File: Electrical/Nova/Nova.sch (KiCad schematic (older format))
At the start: 0 parts

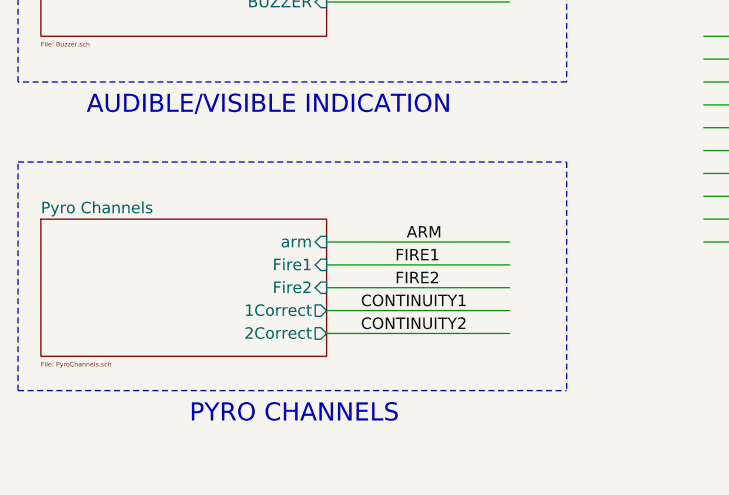
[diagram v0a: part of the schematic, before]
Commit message: Added Third Pyro
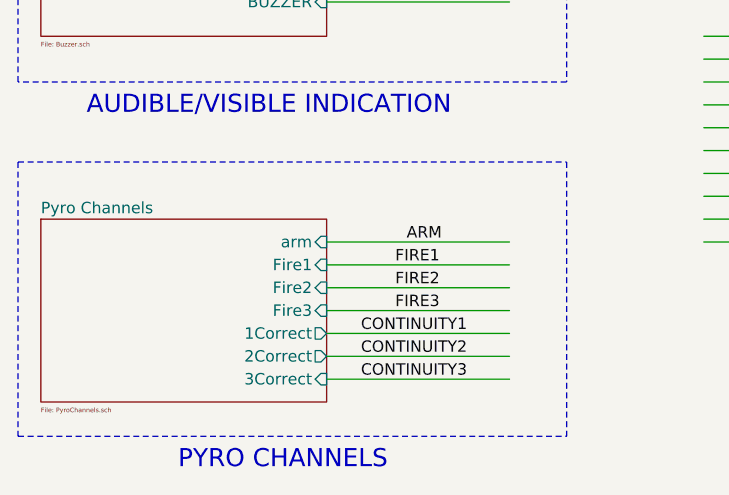
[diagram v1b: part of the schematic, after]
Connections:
- net labels added: CONTINUITY3, FIRE3
- wire segments 99 -> 101
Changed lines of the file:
@@
 $Descr USLetter 11000 8500
 encoding utf-8
-Sheet 1 20
+Sheet 1 21
 Title ""
 Date ""
@@
 	2050 6400 2850 6400
 Wire Wire Line
-	2050 6500 2850 6500
-Wire Wire Line
 	2050 6600 2850 6600
+Wire Wire Line
+	2050 6700 2850 6700
 Text Label 2400 6200 0    50   ~ 0
 ARM
@@
 Text Label 2350 6400 0    50   ~ 0
 FIRE2
-Text Label 2200 6500 0    50   ~ 0
+Text Label 2200 6600 0    50   ~ 0
 CONTINUITY1
-Text Label 2200 6600 0    50   ~ 0
+Text Label 2200 6700 0    50   ~ 0
 CONTINUITY2
 Wire Notes Line
@@
 	700  5850 3100 5850
 Wire Notes Line
-	3100 5850 3100 6850
-Wire Notes Line
-	700  6850 700  5850
-Wire Notes Line
-	700  6850 3100 6850
-Text Notes 1450 7000 0    79   ~ 0
+	700  7050 3100 7050
+Text Notes 1400 7200 0    79   ~ 0
 PYRO CHANNELS
 Wire Notes Line
@@
 	6800 5300 7350 5300
 $Sheet
-S 800  6100 1250 600
+S 800  6100 1250 800
 U 5F448D4B
 F0 "Pyro Channels" 50
@@
 F2 "arm" I R 2050 6200 50
 F3 "Fire1" I R 2050 6300 50
-F4 "1Correct" O R 2050 6500 50
+F4 "1Correct" O R 2050 6600 50
 F5 "Fire2" I R 2050 6400 50
-F6 "2Correct" O R 2050 6600 50
-$EndSheet
+F6 "2Correct" O R 2050 6700 50
+F7 "Fire3" I R 2050 6500 50
+F8 "3Correct" I R 2050 6800 50
+$EndSheet
+Wire Notes Line
+	3100 5850 3100 7050
+Wire Notes Line
+	700  5850 700  7050
+Wire Wire Line
+	2050 6500 2850 6500
+Wire Wire Line
+	2050 6800 2850 6800
+Text Label 2350 6500 0    50   ~ 0
+FIRE3
+Text Label 2200 6800 0    50   ~ 0
+CONTINUITY3
 $EndSCHEMATC

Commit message: Cleaned Up Schematic & Folder for Project
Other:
- note added: "Nova Flight Computer: Rev 1"
- note added: "PIN HEADERS"

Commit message: Changes Galore
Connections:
- net labels added: CS_FLASH, IO0, IO1, IO2, IO3
- net labels removed: HOLD, WP
- no-connect marks 32 -> 30
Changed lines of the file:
@@
 Text Label 8800 950  2    50   ~ 0
 SCLK
-Text Label 8800 1050 2    50   ~ 0
-MOSI
-Text Label 8800 1150 2    50   ~ 0
-MISO
 Text Label 8800 1250 2    50   ~ 0
 BAROMETER_CS
@@
 Text Label 8800 1600 2    50   ~ 0
 SCLK
-Text Label 8800 1700 2    50   ~ 0
-MOSI
-Text Label 8800 1800 2    50   ~ 0
-MISO
 Text Label 8800 1900 2    50   ~ 0
 GYRO_ACCEL_CS
@@
 Text Label 8800 2650 2    50   ~ 0
 SCLK
-Text Label 8800 2550 2    50   ~ 0
-MOSI
-Text Label 8800 2450 2    50   ~ 0
-MISO
 Text Label 8800 2350 2    50   ~ 0
 ACCELEROMETER_CS
@@
 Wire Notes Line
 	3000 5950 3000 4900
-NoConn ~ 8100 4450
-$Sheet
-S 8900 3200 1250 500
-U 5F3B5BD1
-F0 "MicroSD" 50
-F1 "../Common_Modules/FHSD/Flash SD Board/Micro SD.sch" 20
-F2 "MISO" I L 8900 3300 50
-F3 "MOSI" I L 8900 3400 50
-F4 "SCLK" I L 8900 3500 50
-F5 "CS_SD" I L 8900 3600 50
-$EndSheet
-$Sheet
-S 8900 3850 1250 700
-U 5F3B5C2E
-F0 "FlashChip" 50
-F1 "../Common_Modules/FHSD/Flash SD Board/Flash Chip.sch" 20
-F2 "SCLK" I L 8900 3950 50
-F3 "MOSI" I L 8900 4050 50
-F4 "MISO" I L 8900 4150 50
-F5 "CS_FLASH" I L 8900 4250 50
-F6 "HOLD" I L 8900 4350 50
-F7 "WP" I L 8900 4450 50
-$EndSheet
 Text Notes 8900 3100 0    79   ~ 0
 SENSORS\n\n
@@
 DATA LOGGING\n
 Text Label 8800 4250 2    50   ~ 0
-FLASH_CS
+IO2
 Text Label 8800 3600 2    50   ~ 0
 SD_CS
 Text Label 8800 4450 2    50   ~ 0
-WP
+CS_FLASH
 Text Label 8800 4350 2    50   ~ 0
-HOLD
-Text Label 8800 4150 2    50   ~ 0
-MISO
-Text Label 8800 4050 2    50   ~ 0
-MOSI
+IO3
 Text Label 8800 3950 2    50   ~ 0
 SCLK
@@
 F21 "20" I R 2150 6450 50
 $EndSheet
-NoConn ~ 8100 4350
 Wire Notes Line
 	8000 3050 8000 4650
@@
 Text Notes 3350 6000 0    197  ~ 39
 Nova Flight Computer: Rev 1
+Text Label 8800 4150 2    50   ~ 0
+IO1
+Text Label 8800 4050 2    50   ~ 0
+IO0
+$Sheet
+S 8900 3850 1250 700
+U 5F3B5C2E
+F0 "FlashChip" 50
+F1 "../Common_Modules/FHSD/Flash SD Board/Flash Chip.sch" 20
+F2 "SCLK" I L 8900 3950 50
+F3 "IO0" I L 8900 4050 50
+F4 "IO1" I L 8900 4150 50
+F5 "CS_FLASH" I L 8900 4450 50
+F6 "IO3" I L 8900 4350 50
+F7 "IO2" I L 8900 4250 50
+$EndSheet
+$Sheet
+S 8900 3200 1250 500
+U 5F3B5BD1
+F0 "MicroSD" 50
+F1 "../Common_Modules/FHSD/Flash SD Board/Micro SD.sch" 20
+F2 "MISO" I L 8900 3300 50
+F3 "MOSI" I L 8900 3400 50
+F4 "SCLK" I L 8900 3500 50
+F5 "CS_SD" I L 8900 3600 50
+$EndSheet
+Text Label 8800 2550 2    50   ~ 0
+MOSI
+Text Label 8800 2450 2    50   ~ 0
+MISO
+Text Label 8800 1700 2    50   ~ 0
+MOSI
+Text Label 8800 1800 2    50   ~ 0
+MISO
+Text Label 8800 1150 2    50   ~ 0
+MISO
+Text Label 8800 1050 2    50   ~ 0
+MOSI
 $EndSCHEMATC

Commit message: Crossing Fingers Github
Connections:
- wire segments 101 -> 102
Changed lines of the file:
@@
 $Descr USLetter 11000 8500
 encoding utf-8
-Sheet 1 21
+Sheet 1 22
 Title ""
 Date ""
@@
 	8000 3050 10250 3050
 Wire Notes Line
-	10250 4900 10250 5650
-Wire Notes Line
 	750  6200 3000 6200
 Wire Notes Line
@@
 Wire Wire Line
 	2150 2450 2900 2450
-Wire Notes Line
-	8000 5650 8000 4900
-Text Notes 8750 5800 0    79   ~ 0
+Text Notes 8750 6300 0    79   ~ 0
 POWER SUPPLY\n
 $Sheet
-S 8700 5050 1000 500
+S 8900 5050 1250 550
 U 5F3B0B4B
 F0 "PowerSupply" 50
@@
 	8000 4900 10250 4900
 Wire Notes Line
-	8000 5650 10250 5650
+	8000 6150 10250 6150
 NoConn ~ 10150 1600
 NoConn ~ 10150 1700
@@
 Text Label 8800 1050 2    50   ~ 0
 MOSI
+$Sheet
+S 8900 5800 1250 200
+U 5F964042
+F0 "Voltage Monitor" 50
+F1 "Voltage Monitor.sch" 50
+F2 "MonitorPin" I L 8900 5900 50
+$EndSheet
+Wire Notes Line
+	10250 4900 10250 6150
+Wire Notes Line
+	8000 4900 8000 6150
+Wire Wire Line
+	8900 5900 8100 5900
 $EndSCHEMATC

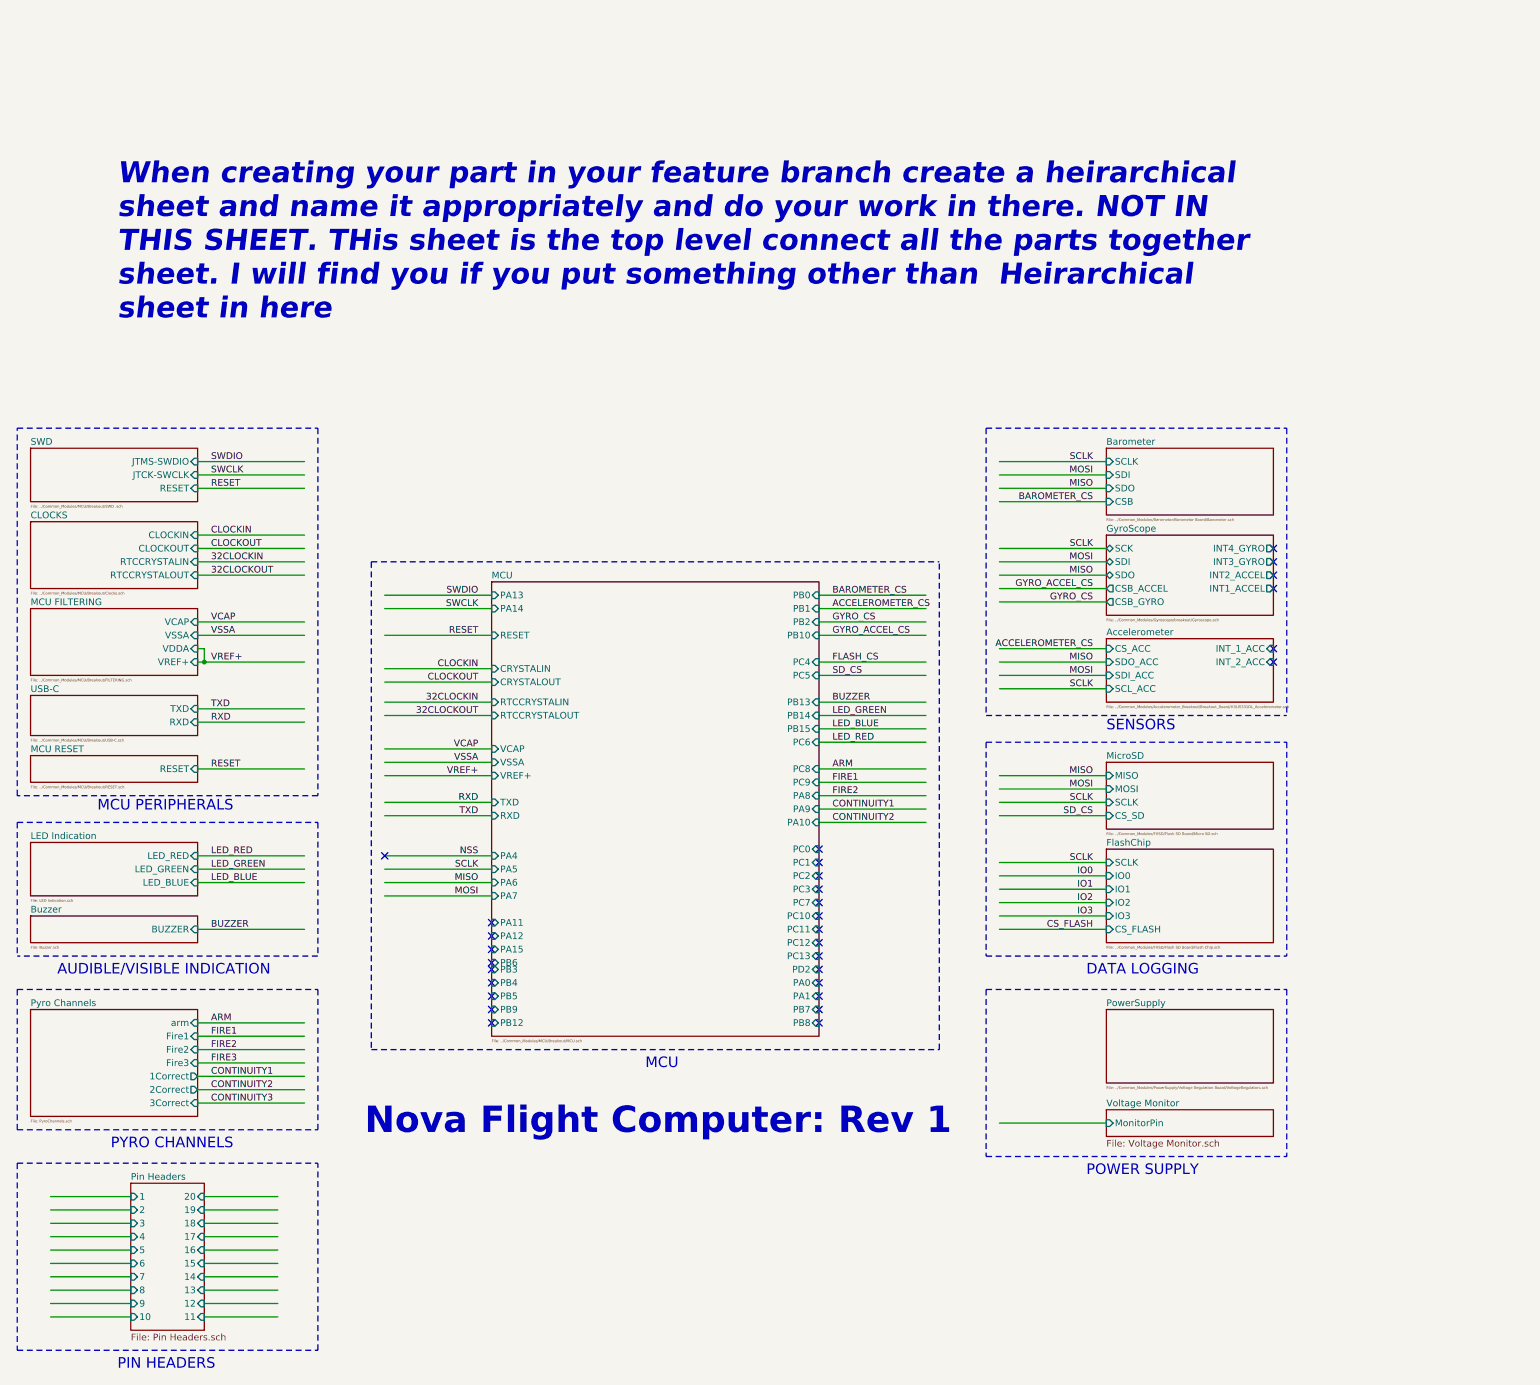
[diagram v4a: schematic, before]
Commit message: A Metric Fuck Ton of Routing + Minor Fixes to Schematic
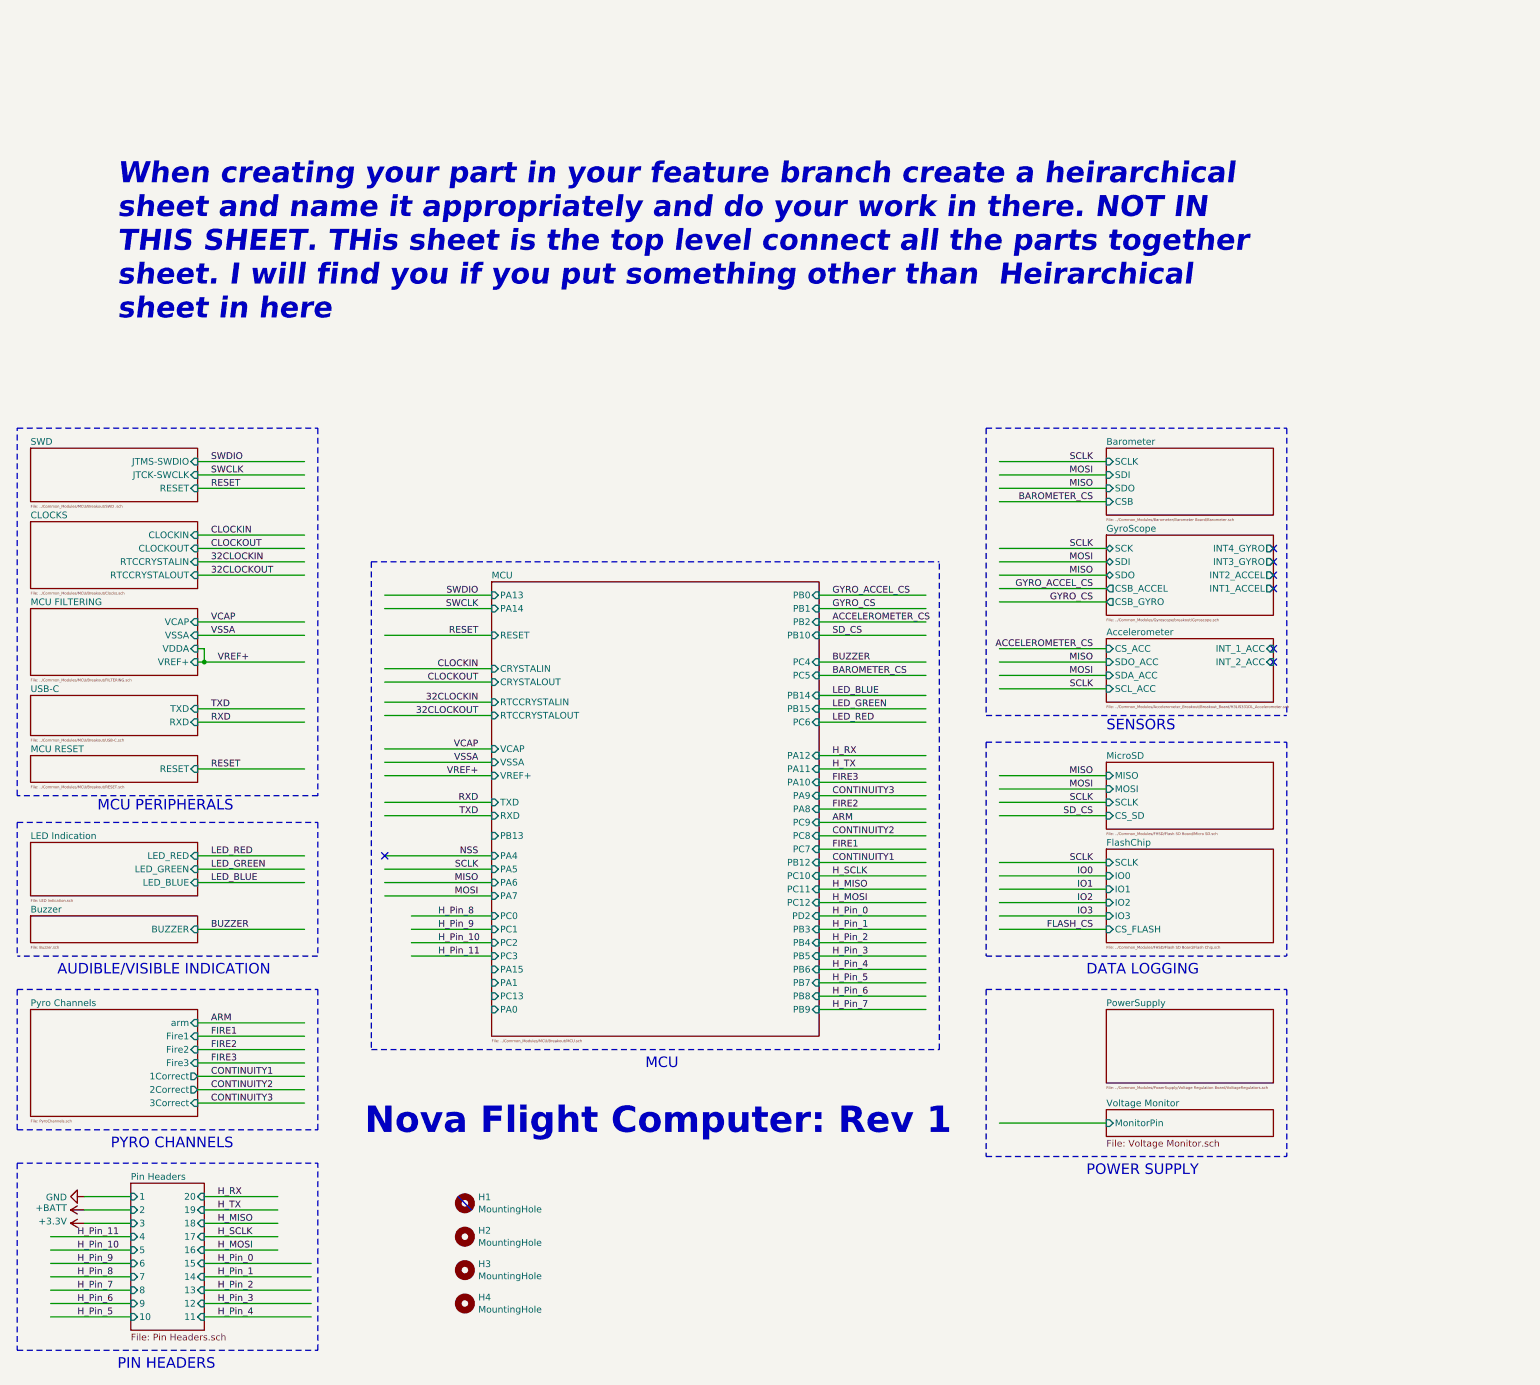
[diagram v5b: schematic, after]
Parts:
- added H1, H2, H3, H4: MountingHole, MountingHole:MountingHole_3mm, symbol Mechanical:MountingHole
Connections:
- net labels added: +3.3V, +BATT, GND, H_MISO, H_MOSI, H_Pin_0, H_Pin_1, H_Pin_10, H_Pin_11, H_Pin_2, H_Pin_3, H_Pin_4, H_Pin_5, H_Pin_6, H_Pin_7, H_Pin_8, H_Pin_9, H_RX, H_SCLK, H_TX
- net labels removed: CS_FLASH
- wire segments 102 -> 120
- no-connect marks 30 -> 7

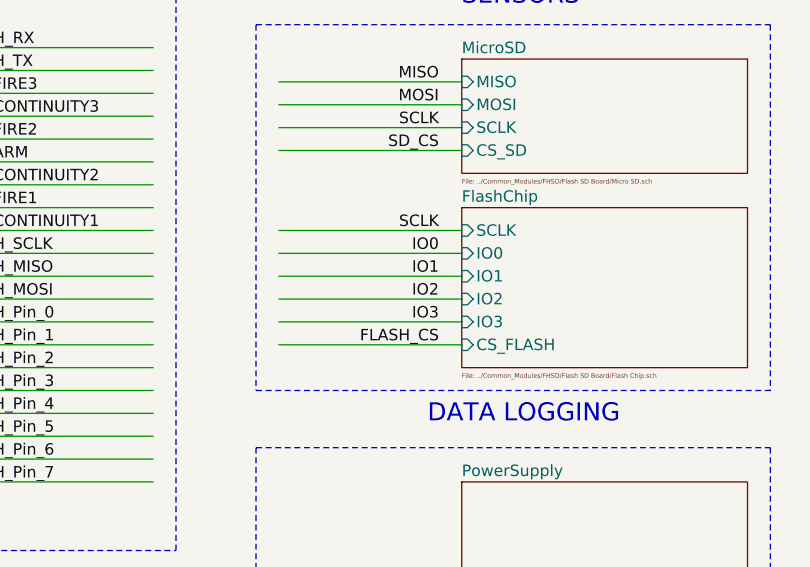
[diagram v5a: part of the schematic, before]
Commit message: Updated the Flash Chip Tracing
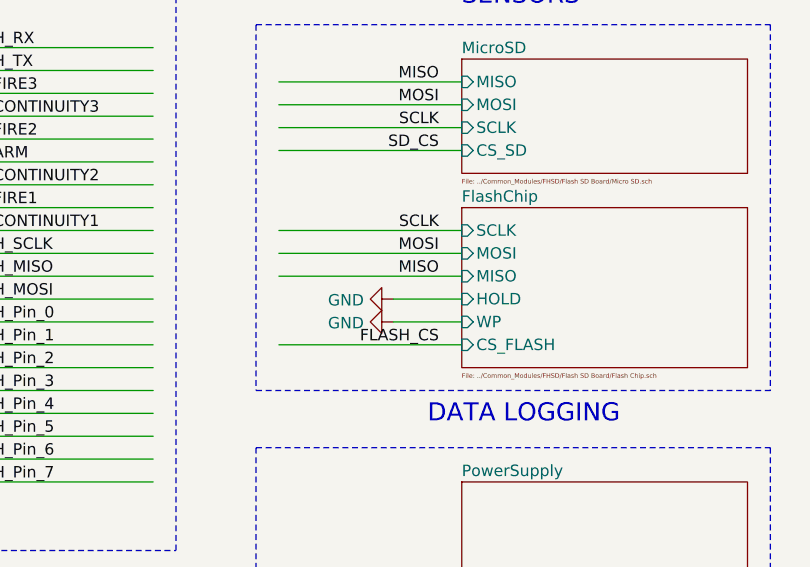
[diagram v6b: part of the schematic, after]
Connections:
- net labels removed: IO0, IO1, IO2, IO3
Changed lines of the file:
@@
 Text Notes 8750 4800 0    79   ~ 0
 DATA LOGGING\n
-Text Label 8800 4250 2    50   ~ 0
-IO2
 Text Label 8800 3600 2    50   ~ 0
 SD_CS
 Text Label 8800 4450 2    50   ~ 0
 FLASH_CS
-Text Label 8800 4350 2    50   ~ 0
-IO3
 Text Label 8800 3950 2    50   ~ 0
 SCLK
@@
 Wire Wire Line
 	8900 4450 8100 4450
-Wire Wire Line
-	8900 4350 8100 4350
-Wire Wire Line
-	8100 4250 8900 4250
 Wire Wire Line
 	8900 4150 8100 4150
@@
 Text Notes 3350 6000 0    197  ~ 39
 Nova Flight Computer: Rev 1
-Text Label 8800 4150 2    50   ~ 0
-IO1
-Text Label 8800 4050 2    50   ~ 0
-IO0
-$Sheet
-S 8900 3850 1250 700
-U 5F3B5C2E
-F0 "FlashChip" 50
-F1 "../Common_Modules/FHSD/Flash SD Board/Flash Chip.sch" 20
-F2 "SCLK" I L 8900 3950 50
-F3 "IO0" I L 8900 4050 50
-F4 "IO1" I L 8900 4150 50
-F5 "CS_FLASH" I L 8900 4450 50
-F6 "IO3" I L 8900 4350 50
-F7 "IO2" I L 8900 4250 50
-$EndSheet
 $Sheet
 S 8900 3200 1250 500
@@
 Text Label 3900 4650 0    50   ~ 0
 H_Pin_11
+$Sheet
+S 8900 3850 1250 700
+U 5F3B5C2E
+F0 "FlashChip" 50
+F1 "../Common_Modules/FHSD/Flash SD Board/Flash Chip.sch" 20
+F2 "SCLK" I L 8900 3950 50
+F3 "CS_FLASH" I L 8900 4450 50
+F4 "MOSI" I L 8900 4050 50
+F5 "MISO" I L 8900 4150 50
+F6 "HOLD" I L 8900 4250 50
+F7 "WP" I L 8900 4350 50
+$EndSheet
+Text Label 8800 4150 2    50   ~ 0
+MISO
+Text Label 8800 4050 2    50   ~ 0
+MOSI
+$Comp
+L power:GND #PWR?
+U 1 1 5FA3956D
+P 8600 4250
+F 0 "#PWR?" H 8600 4000 50  0001 C CNN
+F 1 "GND" V 8605 4122 50  0000 R CNN
+F 2 "" H 8600 4250 50  0001 C CNN
+F 3 "" H 8600 4250 50  0001 C CNN
+	1    8600 4250
+	0    1    1    0
+$EndComp
+$Comp
+L power:GND #PWR?
+U 1 1 5FA39A9B
+P 8600 4350
+F 0 "#PWR?" H 8600 4100 50  0001 C CNN
+F 1 "GND" V 8605 4222 50  0000 R CNN
+F 2 "" H 8600 4350 50  0001 C CNN
+F 3 "" H 8600 4350 50  0001 C CNN
+	1    8600 4350
+	0    1    1    0
+$EndComp
+Wire Wire Line
+	8900 4250 8600 4250
+Wire Wire Line
+	8600 4350 8900 4350
 $EndSCHEMATC
